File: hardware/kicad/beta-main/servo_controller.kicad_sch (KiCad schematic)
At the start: 12 parts, among them J2 Servo Socket, J3 Servo Socket, J4 Servo Socket, J5 Servo Socket, Q1 MMBT3906, U1 74LVC1G126, U2 74LVC1G126

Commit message: 5V and amplifier corrections
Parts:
- renumbered J2 to J4, J3 to J5, J4 to J6, J5 to J7, R5 to R10, R3 to R6, R2 to R7, R1 to R8, R4 to R9, U1 to U4, U2 to U5
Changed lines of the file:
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@@
-	(wire
-		(pts
-			(xy 100.33 59.69) (xy 99.06 59.69)
-		)
-		(stroke
-			(width 0)
-			(type default)
-		)
-	)
 	(wire
 		(pts
@@
 	(hierarchical_label "3V3"
 		(shape input)
-		(at 99.06 59.69 90)
+		(at 100.33 59.69 90)
 		(effects
 			(font
@@
 		(on_board yes)
 		(dnp no)
-		(property "Reference" "R4"
+		(property "Reference" "R9"
 			(at 123.19 62.2299 0)
 			(effects
@@
 			(project "beta-main"
 				(path "/ec75fd42-4efa-4f32-b57e-76d632cb46f5/c35ad228-8cfd-4958-93e3-246eeca4dc8e"
-					(reference "R4")
+					(reference "R9")
 					(unit 1)
 				)
@@
 		(dnp no)
 		(fields_autoplaced yes)
-		(property "Reference" "R3"
+		(property "Reference" "R6"
 			(at 66.04 82.5499 0)
 			(effects
@@
 			(project "beta-main"
 				(path "/ec75fd42-4efa-4f32-b57e-76d632cb46f5/c35ad228-8cfd-4958-93e3-246eeca4dc8e"
-					(reference "R3")
+					(reference "R6")
 					(unit 1)
 				)
@@
 		(on_board yes)
 		(dnp no)
-		(property "Reference" "J3"
+		(property "Reference" "J5"
 			(at 187.96 63.5001 0)
 			(effects
@@
 			(project "beta-main"
 				(path "/ec75fd42-4efa-4f32-b57e-76d632cb46f5/c35ad228-8cfd-4958-93e3-246eeca4dc8e"
-					(reference "J3")
+					(reference "J5")
 					(unit 1)
 				)
@@
 		(on_board yes)
 		(dnp no)
-		(property "Reference" "U2"
+		(property "Reference" "U5"
 			(at 139.954 73.914 0)
 			(effects
@@
 			(project "beta-main"
 				(path "/ec75fd42-4efa-4f32-b57e-76d632cb46f5/c35ad228-8cfd-4958-93e3-246eeca4dc8e"
-					(reference "U2")
+					(reference "U5")
 					(unit 1)
 				)
@@
 		(on_board yes)
 		(dnp no)
-		(property "Reference" "J4"
+		(property "Reference" "J6"
 			(at 187.96 76.2001 0)
 			(effects
@@
 			(project "beta-main"
 				(path "/ec75fd42-4efa-4f32-b57e-76d632cb46f5/c35ad228-8cfd-4958-93e3-246eeca4dc8e"
-					(reference "J4")
+					(reference "J6")
 					(unit 1)
 				)
@@
 		(on_board yes)
 		(dnp no)
-		(property "Reference" "R5"
+		(property "Reference" "R10"
 			(at 156.21 62.2299 0)
 			(effects
@@
 			(project "beta-main"
 				(path "/ec75fd42-4efa-4f32-b57e-76d632cb46f5/c35ad228-8cfd-4958-93e3-246eeca4dc8e"
-					(reference "R5")
+					(reference "R10")
 					(unit 1)
 				)
@@
 		(dnp no)
 		(fields_autoplaced yes)
-		(property "Reference" "R2"
+		(property "Reference" "R7"
 			(at 76.2 63.5 90)
 			(effects
@@
 			(project "beta-main"
 				(path "/ec75fd42-4efa-4f32-b57e-76d632cb46f5/c35ad228-8cfd-4958-93e3-246eeca4dc8e"
-					(reference "R2")
+					(reference "R7")
 					(unit 1)
 				)
@@
 		(on_board yes)
 		(dnp no)
-		(property "Reference" "R1"
+		(property "Reference" "R8"
 			(at 83.82 62.2299 0)
 			(effects
@@
 			(project "beta-main"
 				(path "/ec75fd42-4efa-4f32-b57e-76d632cb46f5/c35ad228-8cfd-4958-93e3-246eeca4dc8e"
-					(reference "R1")
+					(reference "R8")
 					(unit 1)
 				)
@@
 		(on_board yes)
 		(dnp no)
-		(property "Reference" "J5"
+		(property "Reference" "J7"
 			(at 187.96 88.9001 0)
 			(effects
@@
 			(project "beta-main"
 				(path "/ec75fd42-4efa-4f32-b57e-76d632cb46f5/c35ad228-8cfd-4958-93e3-246eeca4dc8e"
-					(reference "J5")
+					(reference "J7")
 					(unit 1)
 				)
@@
 		(on_board yes)
 		(dnp no)
-		(property "Reference" "U1"
+		(property "Reference" "U4"
 			(at 105.41 74.422 0)
 			(effects
@@
 			(project "beta-main"
 				(path "/ec75fd42-4efa-4f32-b57e-76d632cb46f5/c35ad228-8cfd-4958-93e3-246eeca4dc8e"
-					(reference "U1")
+					(reference "U4")
 					(unit 1)
 				)
@@
 		(on_board yes)
 		(dnp no)
-		(property "Reference" "J2"
+		(property "Reference" "J4"
 			(at 187.96 53.3401 0)
 			(effects
@@
 			(project "beta-main"
 				(path "/ec75fd42-4efa-4f32-b57e-76d632cb46f5/c35ad228-8cfd-4958-93e3-246eeca4dc8e"
-					(reference "J2")
+					(reference "J4")
 					(unit 1)
 				)

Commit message: Setup for PCB layout
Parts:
- J4, J5, J6, J7: footprint (none) -> Connector_PinHeader_2.54mm:PinHeader_1x03_P2.54mm_Vertical
- R10, R6, R7, R8, R9: footprint (none) -> Resistor_SMD:R_0402_1005Metric
- U4, U5: footprint (none) -> Package_TO_SOT_SMD:SOT-23-5
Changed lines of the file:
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@@
 			)
 		)
-		(property "Footprint" ""
+		(property "Footprint" "Resistor_SMD:R_0402_1005Metric"
 			(at 118.872 63.5 90)
 			(effects
@@
 			)
 		)
-		(property "Footprint" ""
+		(property "Footprint" "Resistor_SMD:R_0402_1005Metric"
 			(at 65.278 83.82 90)
 			(effects
@@
 			)
 		)
-		(property "Footprint" ""
+		(property "Footprint" "Connector_PinHeader_2.54mm:PinHeader_1x03_P2.54mm_Vertical"
 			(at 186.69 62.23 0)
 			(effects
@@
 			)
 		)
-		(property "Footprint" ""
+		(property "Footprint" "Package_TO_SOT_SMD:SOT-23-5"
 			(at 138.43 69.85 0)
 			(effects
@@
 			)
 		)
-		(property "Footprint" ""
+		(property "Footprint" "Connector_PinHeader_2.54mm:PinHeader_1x03_P2.54mm_Vertical"
 			(at 186.69 74.93 0)
 			(effects
@@
 			)
 		)
-		(property "Footprint" ""
+		(property "Footprint" "Resistor_SMD:R_0402_1005Metric"
 			(at 151.892 63.5 90)
 			(effects
@@
 			)
 		)
-		(property "Footprint" ""
+		(property "Footprint" "Resistor_SMD:R_0402_1005Metric"
 			(at 76.2 71.628 90)
 			(effects
@@
 			)
 		)
-		(property "Footprint" ""
+		(property "Footprint" "Resistor_SMD:R_0402_1005Metric"
 			(at 79.502 63.5 90)
 			(effects
@@
 			)
 		)
-		(property "Footprint" ""
+		(property "Footprint" "Connector_PinHeader_2.54mm:PinHeader_1x03_P2.54mm_Vertical"
 			(at 186.69 87.63 0)
 			(effects
@@
 			)
 		)
-		(property "Footprint" ""
+		(property "Footprint" "Package_TO_SOT_SMD:SOT-23-5"
 			(at 105.41 69.85 0)
 			(effects
@@
 			)
 		)
-		(property "Footprint" ""
+		(property "Footprint" "Connector_PinHeader_2.54mm:PinHeader_1x03_P2.54mm_Vertical"
 			(at 186.69 52.07 0)
 			(effects

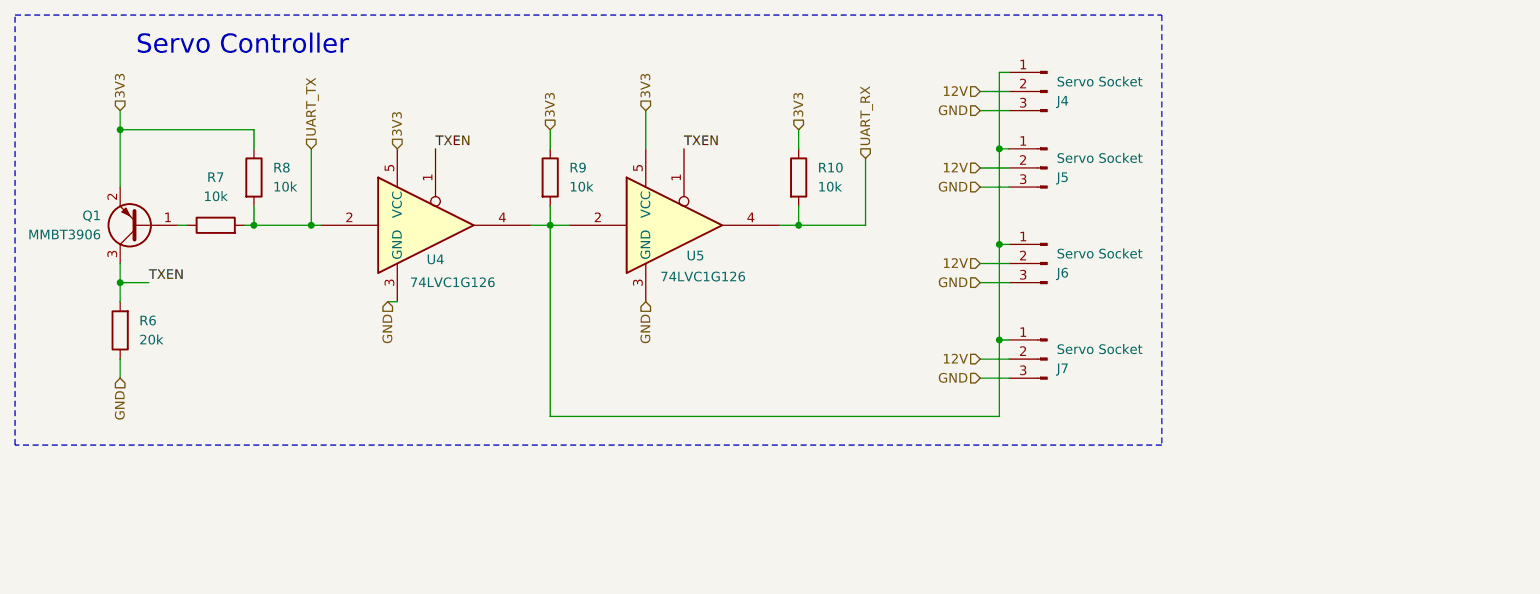
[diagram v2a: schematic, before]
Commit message: remove power symbols from hierarchy and move different subsystems  around
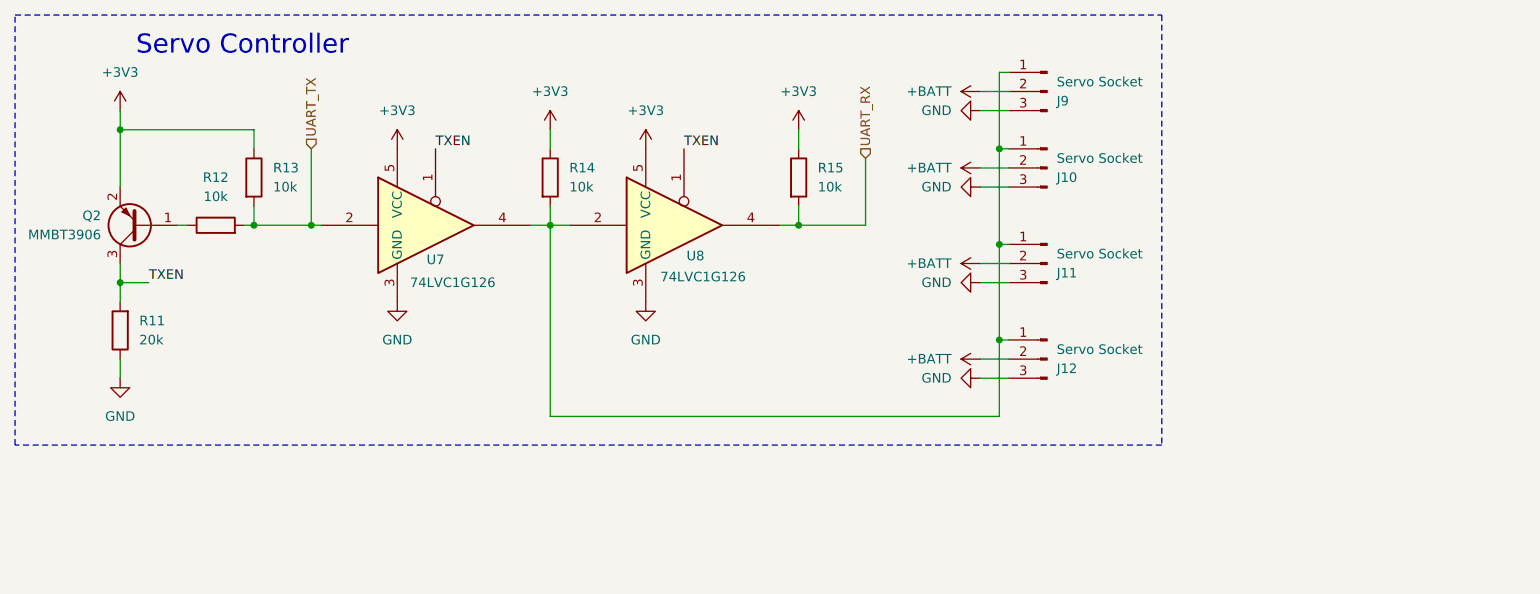
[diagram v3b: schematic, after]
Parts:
- renumbered J5 to J10, J6 to J11, J7 to J12, J4 to J9, Q1 to Q2, R6 to R11, R7 to R12, R8 to R13, R9 to R14, R10 to R15, U4 to U7, U5 to U8
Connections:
- net 12V renamed +BATT
- net 3V3 renamed +3V3

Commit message: create template for components placement with drawn contraints
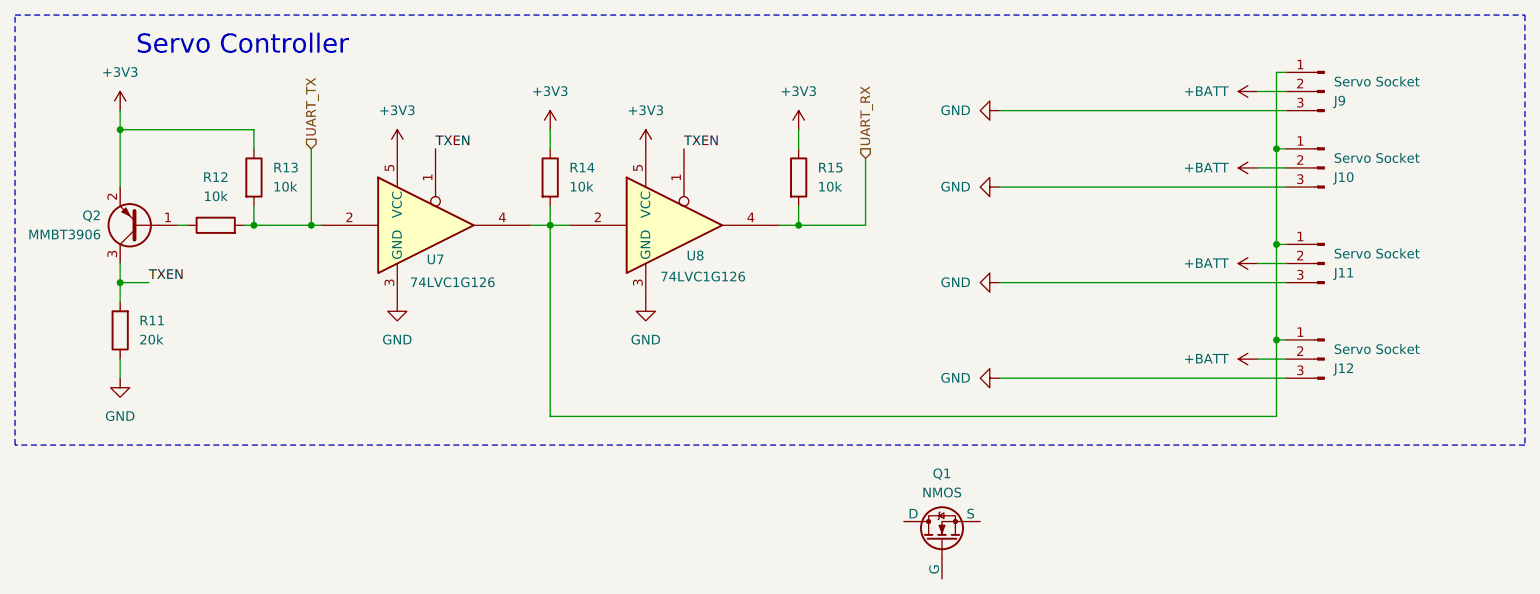
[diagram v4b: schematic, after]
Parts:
- added Q1: NMOS, symbol Simulation_SPICE:NMOS
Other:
- moved on the sheet: J10, J11, J12, J9

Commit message: Footprints fixed, fuse removed
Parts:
- J10, J11, J12, J9: footprint Connector_PinHeader_2.54mm:PinHeader_1x03_P2.54mm_Vertical -> Connector_JST:JST_XH_B3B-XH-AM_1x03_P2.50mm_Vertical
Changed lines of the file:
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@@
 			)
 		)
-		(property "Footprint" "Connector_PinHeader_2.54mm:PinHeader_1x03_P2.54mm_Vertical"
+		(property "Footprint" "Connector_JST:JST_XH_B3B-XH-AM_1x03_P2.50mm_Vertical"
 			(at 223.52 62.23 0)
 			(effects
@@
 			)
 		)
-		(property "Footprint" "Connector_PinHeader_2.54mm:PinHeader_1x03_P2.54mm_Vertical"
+		(property "Footprint" "Connector_JST:JST_XH_B3B-XH-AM_1x03_P2.50mm_Vertical"
 			(at 223.52 74.93 0)
 			(effects
@@
 			)
 		)
-		(property "Footprint" "Connector_PinHeader_2.54mm:PinHeader_1x03_P2.54mm_Vertical"
+		(property "Footprint" "Connector_JST:JST_XH_B3B-XH-AM_1x03_P2.50mm_Vertical"
 			(at 223.52 87.63 0)
 			(effects
@@
 			)
 		)
-		(property "Footprint" "Connector_PinHeader_2.54mm:PinHeader_1x03_P2.54mm_Vertical"
+		(property "Footprint" "Connector_JST:JST_XH_B3B-XH-AM_1x03_P2.50mm_Vertical"
 			(at 223.52 52.07 0)
 			(effects
